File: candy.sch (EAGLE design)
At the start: 4 parts

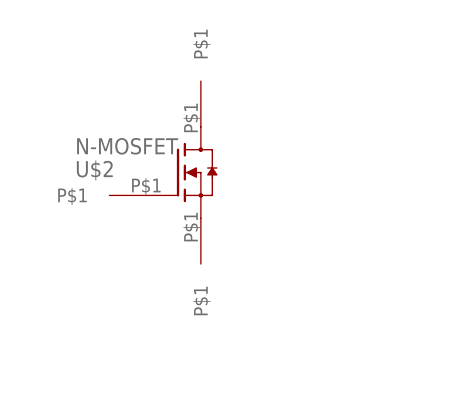
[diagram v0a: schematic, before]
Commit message: has candy, too big pads
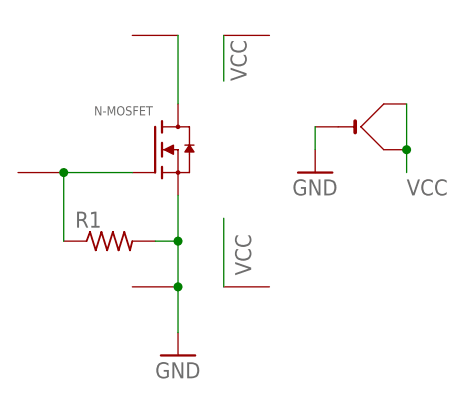
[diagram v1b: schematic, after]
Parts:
- added R1: (no value), adafruit:R-US_R1206
- added U$5, U$6: SMDPAD, TinyTony_ShenzenReady:SMDPAD
- added U$7: (no value), TinyTony_ShenzenReady:CR2032
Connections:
- removed net N$2: U$2.S, U$3.P$1
- new net GND: R1.2, U$2.S, U$3.P$1, U$7.-
- new net VCC: U$5.P$1, U$6.P$1, U$7.+, U$7.+1
- net N$1: now also R1.1
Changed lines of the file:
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@@
 <?xml version="1.0" encoding="utf-8"?>
 <!DOCTYPE eagle SYSTEM "eagle.dtd">
-<eagle version="8.7.0">
+<eagle version="8.6.0">
 <drawing>
 <settings>
@@
 <part name="U$3" library="TinyTony_ShenzenReady" deviceset="SMDPAD" device=""/>
 <part name="U$4" library="TinyTony_ShenzenReady" deviceset="SMDPAD" device=""/>
+<part name="R1" library="adafruit" library_urn="urn:adsk.eagle:library:420" deviceset="R-US_" device="R1206"/>
+<part name="U$5" library="TinyTony_ShenzenReady" deviceset="SMDPAD" device=""/>
+<part name="U$6" library="TinyTony_ShenzenReady" deviceset="SMDPAD" device=""/>
+<part name="U$7" library="TinyTony_ShenzenReady" deviceset="CR2032" device=""/>
+<part name="GND1" library="TinyTony_ShenzenReady" deviceset="GND" device=""/>
+<part name="GND2" library="TinyTony_ShenzenReady" deviceset="GND" device=""/>
 </parts>
 <sheets>
@@
 </plain>
 <instances>
-<instance part="U$1" gate="G$1" x="73.66" y="55.88" rot="R180"/>
-<instance part="U$2" gate="G$1" x="76.2" y="58.42"/>
-<instance part="U$3" gate="G$1" x="78.74" y="53.34" rot="R270"/>
-<instance part="U$4" gate="G$1" x="78.74" y="63.5" rot="R90"/>
+<instance part="U$1" gate="G$1" x="63.5" y="58.42" rot="R180"/>
+<instance part="U$2" gate="G$1" x="73.66" y="60.96" smashed="yes">
+<attribute name="VALUE" x="73.406" y="64.77" size="1.016" layer="96" rot="MR0"/>
+</instance>
+<instance part="U$3" gate="G$1" x="76.2" y="45.72" smashed="yes" rot="R180"/>
+<instance part="U$4" gate="G$1" x="76.2" y="73.66" smashed="yes" rot="R180"/>
+<instance part="R1" gate="G$1" x="68.58" y="50.8"/>
+<instance part="U$5" gate="G$1" x="81.28" y="73.66" smashed="yes"/>
+<instance part="U$6" gate="G$1" x="81.28" y="45.72" smashed="yes"/>
+<instance part="U$7" gate="G$1" x="96.52" y="63.5" smashed="yes">
+<attribute name="VALUE" x="95.25" y="58.42" size="1.778" layer="96"/>
+</instance>
+<instance part="GND1" gate="1" x="91.44" y="58.42"/>
+<instance part="GND2" gate="1" x="76.2" y="38.1"/>
 </instances>
 <busses>
@@
 <pinref part="U$2" gate="G$1" pin="G"/>
 <pinref part="U$1" gate="G$1" pin="P$1"/>
-</segment>
-</net>
-<net name="N$2" class="0">
+<wire x1="63.5" y1="58.42" x2="71.12" y2="58.42" width="0.1524" layer="91"/>
+<pinref part="R1" gate="G$1" pin="1"/>
+<wire x1="63.5" y1="50.8" x2="63.5" y2="58.42" width="0.1524" layer="91"/>
+<junction x="63.5" y="58.42"/>
+</segment>
+</net>
+<net name="N$3" class="0">
+<segment>
+<pinref part="U$2" gate="G$1" pin="D"/>
+<pinref part="U$4" gate="G$1" pin="P$1"/>
+<wire x1="76.2" y1="73.66" x2="76.2" y2="66.04" width="0.1524" layer="91"/>
+</segment>
+</net>
+<net name="GND" class="0">
+<segment>
+<pinref part="U$7" gate="G$1" pin="-"/>
+<pinref part="GND1" gate="1" pin="GND"/>
+<wire x1="91.44" y1="60.96" x2="91.44" y2="63.5" width="0.1524" layer="91"/>
+</segment>
 <segment>
 <pinref part="U$2" gate="G$1" pin="S"/>
 <pinref part="U$3" gate="G$1" pin="P$1"/>
-</segment>
-</net>
-<net name="N$3" class="0">
-<segment>
-<pinref part="U$2" gate="G$1" pin="D"/>
-<pinref part="U$4" gate="G$1" pin="P$1"/>
+<pinref part="R1" gate="G$1" pin="2"/>
+<wire x1="76.2" y1="50.8" x2="76.2" y2="55.88" width="0.1524" layer="91"/>
+<wire x1="76.2" y1="50.8" x2="73.66" y2="50.8" width="0.1524" layer="91"/>
+<junction x="76.2" y="50.8"/>
+<wire x1="76.2" y1="45.72" x2="76.2" y2="50.8" width="0.1524" layer="91"/>
+<pinref part="GND2" gate="1" pin="GND"/>
+<wire x1="76.2" y1="45.72" x2="76.2" y2="40.64" width="0.1524" layer="91"/>
+<junction x="76.2" y="45.72"/>
+</segment>
+</net>
+<net name="VCC" class="0">
+<segment>
+<label x="101.6" y="55.88" size="1.778" layer="95"/>
+<pinref part="U$7" gate="G$1" pin="+1"/>
+<wire x1="101.6" y1="60.96" x2="101.6" y2="58.42" width="0.1524" layer="91"/>
+<pinref part="U$7" gate="G$1" pin="+"/>
+<wire x1="101.6" y1="66.04" x2="101.6" y2="60.96" width="0.1524" layer="91"/>
+<junction x="101.6" y="60.96"/>
+</segment>
+<segment>
+<pinref part="U$5" gate="G$1" pin="P$1"/>
+<wire x1="81.28" y1="73.66" x2="81.28" y2="68.58" width="0.1524" layer="91"/>
+<label x="82.042" y="73.152" size="1.778" layer="95" rot="R270"/>
+</segment>
+<segment>
+<pinref part="U$6" gate="G$1" pin="P$1"/>
+<wire x1="81.28" y1="45.72" x2="81.28" y2="53.34" width="0.1524" layer="91"/>
+<label x="82.55" y="51.562" size="1.778" layer="95" rot="R270"/>
 </segment>
 </net>
@@
 </drawing>
 <compatibility>
+<note version="8.2" severity="warning">
+Since Version 8.2, EAGLE supports online libraries. The ids
+of those online libraries will not be understood (or retained)
+with this version.
+</note>
 <note version="8.3" severity="warning">
 Since Version 8.3, EAGLE supports URNs for individual library

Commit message: sch
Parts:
- U$2: value N-MOSFET -> N-MOSFETREGULAR; device TinyTony_ShenzenReady:N-MOSFET -> TinyTony_ShenzenReady:N-MOSFETREGULAR
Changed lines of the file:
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@@
 <parts>
 <part name="U$1" library="TinyTony_ShenzenReady" deviceset="SMDPAD" device=""/>
-<part name="U$2" library="TinyTony_ShenzenReady" deviceset="N-MOSFET" device=""/>
+<part name="U$2" library="TinyTony_ShenzenReady" deviceset="N-MOSFET" device="REGULAR" value="N-MOSFETREGULAR"/>
 <part name="U$3" library="TinyTony_ShenzenReady" deviceset="SMDPAD" device=""/>
 <part name="U$4" library="TinyTony_ShenzenReady" deviceset="SMDPAD" device=""/>

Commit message: with ugly polygons on layout
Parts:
- U$7: device TinyTony_ShenzenReady:CR2032 -> TinyTony_ShenzenReady:CR2032LINX
- renumbered U$6 to VCC
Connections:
- net VCC: no longer U$7.+1
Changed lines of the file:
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@@
 <?xml version="1.0" encoding="utf-8"?>
 <!DOCTYPE eagle SYSTEM "eagle.dtd">
-<eagle version="8.6.0">
+<eagle version="8.7.0">
 <drawing>
 <settings>
@@
 <grid distance="0.1" unitdist="inch" unit="inch" style="lines" multiple="1" display="no" altdistance="0.01" altunitdist="inch" altunit="inch"/>
 <layers>
-<layer number="1" name="Top" color="4" fill="1" visible="no" active="no"/>
-<layer number="16" name="Bottom" color="1" fill="1" visible="no" active="no"/>
-<layer number="17" name="Pads" color="2" fill="1" visible="no" active="no"/>
-<layer number="18" name="Vias" color="2" fill="1" visible="no" active="no"/>
-<layer number="19" name="Unrouted" color="6" fill="1" visible="no" active="no"/>
-<layer number="20" name="Dimension" color="15" fill="1" visible="no" active="no"/>
-<layer number="21" name="tPlace" color="7" fill="1" visible="no" active="no"/>
-<layer number="22" name="bPlace" color="7" fill="1" visible="no" active="no"/>
-<layer number="23" name="tOrigins" color="15" fill="1" visible="no" active="no"/>
-<layer number="24" name="bOrigins" color="15" fill="1" visible="no" active="no"/>
-<layer number="25" name="tNames" color="7" fill="1" visible="no" active="no"/>
-<layer number="26" name="bNames" color="7" fill="1" visible="no" active="no"/>
-<layer number="27" name="tValues" color="7" fill="1" visible="no" active="no"/>
-<layer number="28" name="bValues" color="7" fill="1" visible="no" active="no"/>
+<layer number="1" name="Top" color="4" fill="1" visible="yes" active="no"/>
+<layer number="16" name="Bottom" color="1" fill="1" visible="yes" active="no"/>
+<layer number="17" name="Pads" color="2" fill="1" visible="yes" active="no"/>
+<layer number="18" name="Vias" color="2" fill="1" visible="yes" active="no"/>
+<layer number="19" name="Unrouted" color="6" fill="1" visible="yes" active="no"/>
+<layer number="20" name="Dimension" color="24" fill="1" visible="yes" active="no"/>
+<layer number="21" name="tPlace" color="7" fill="1" visible="yes" active="no"/>
+<layer number="22" name="bPlace" color="7" fill="1" visible="yes" active="no"/>
+<layer number="23" name="tOrigins" color="15" fill="1" visible="yes" active="no"/>
+<layer number="24" name="bOrigins" color="15" fill="1" visible="yes" active="no"/>
+<layer number="25" name="tNames" color="7" fill="1" visible="yes" active="no"/>
+<layer number="26" name="bNames" color="7" fill="1" visible="yes" active="no"/>
+<layer number="27" name="tValues" color="7" fill="1" visible="yes" active="no"/>
+<layer number="28" name="bValues" color="7" fill="1" visible="yes" active="no"/>
 <layer number="29" name="tStop" color="7" fill="3" visible="no" active="no"/>
 <layer number="30" name="bStop" color="7" fill="6" visible="no" active="no"/>
@@
 <layer number="35" name="tGlue" color="7" fill="4" visible="no" active="no"/>
 <layer number="36" name="bGlue" color="7" fill="5" visible="no" active="no"/>
-<layer number="37" name="tTest" color="7" fill="1" visible="no" active="no"/>
-<layer number="38" name="bTest" color="7" fill="1" visible="no" active="no"/>
+<layer number="37" name="tTest" color="7" fill="1" visible="yes" active="no"/>
+<layer number="38" name="bTest" color="7" fill="1" visible="yes" active="no"/>
 <layer number="39" name="tKeepout" color="4" fill="11" visible="no" active="no"/>
 <layer number="40" name="bKeepout" color="1" fill="11" visible="no" active="no"/>
@@
 <layer number="44" name="Drills" color="7" fill="1" visible="no" active="no"/>
 <layer number="45" name="Holes" color="7" fill="1" visible="no" active="no"/>
-<layer number="46" name="Milling" color="3" fill="1" visible="no" active="no"/>
-<layer number="47" name="Measures" color="7" fill="1" visible="no" active="no"/>
-<layer number="48" name="Document" color="7" fill="1" visible="no" active="no"/>
-<layer number="49" name="Reference" color="7" fill="1" visible="no" active="no"/>
-<layer number="50" name="dxf" color="7" fill="1" visible="no" active="no"/>
-<layer number="51" name="tDocu" color="7" fill="1" visible="no" active="no"/>
-<layer number="52" name="bDocu" color="7" fill="1" visible="no" active="no"/>
-<layer number="53" name="tGND_GNDA" color="7" fill="1" visible="no" active="no"/>
-<layer number="54" name="bGND_GNDA" color="7" fill="1" visible="no" active="no"/>
-<layer number="56" name="wert" color="7" fill="1" visible="no" active="no"/>
-<layer number="57" name="tCAD" color="7" fill="1" visible="no" active="no"/>
-<layer number="59" name="tCarbon" color="7" fill="1" visible="no" active="no"/>
-<layer number="60" name="bCarbon" color="7" fill="1" visible="no" active="no"/>
+<layer number="46" name="Milling" color="3" fill="1" visible="yes" active="no"/>
+<layer number="47" name="Measures" color="7" fill="1" visible="yes" active="no"/>
+<layer number="48" name="Document" color="7" fill="1" visible="yes" active="no"/>
+<layer number="49" name="Reference" color="7" fill="1" visible="yes" active="no"/>
+<layer number="50" name="dxf" color="7" fill="1" visible="yes" active="no"/>
+<layer number="51" name="tDocu" color="7" fill="1" visible="yes" active="no"/>
+<layer number="52" name="bDocu" color="7" fill="1" visible="yes" active="no"/>
+<layer number="53" name="tGND_GNDA" color="7" fill="1" visible="yes" active="no"/>
+<layer number="54" name="bGND_GNDA" color="7" fill="1" visible="yes" active="no"/>
+<layer number="56" name="wert" color="7" fill="1" visible="yes" active="no"/>
+<layer number="57" name="tCAD" color="7" fill="1" visible="yes" active="no"/>
+<layer number="59" name="tCarbon" color="7" fill="1" visible="yes" active="no"/>
+<layer number="60" name="bCarbon" color="7" fill="1" visible="yes" active="no"/>
 <layer number="88" name="SimResults" color="9" fill="1" visible="yes" active="yes"/>
 <layer number="89" name="SimProbes" color="9" fill="1" visible="yes" active="yes"/>
@@
 <part name="R1" library="adafruit" library_urn="urn:adsk.eagle:library:420" deviceset="R-US_" device="R1206"/>
 <part name="U$5" library="TinyTony_ShenzenReady" deviceset="SMDPAD" device=""/>
-<part name="U$6" library="TinyTony_ShenzenReady" deviceset="SMDPAD" device=""/>
-<part name="U$7" library="TinyTony_ShenzenReady" deviceset="CR2032" device=""/>
+<part name="VCC" library="TinyTony_ShenzenReady" deviceset="SMDPAD" device=""/>
+<part name="U$7" library="TinyTony_ShenzenReady" library_urn="urn:adsk.eagle:library:2159173" deviceset="CR2032" device="LINX" package3d_urn="urn:adsk.eagle:package:2160680/2"/>
 <part name="GND1" library="TinyTony_ShenzenReady" deviceset="GND" device=""/>
 <part name="GND2" library="TinyTony_ShenzenReady" deviceset="GND" device=""/>
@@
 <instance part="R1" gate="G$1" x="68.58" y="50.8"/>
 <instance part="U$5" gate="G$1" x="81.28" y="73.66" smashed="yes"/>
-<instance part="U$6" gate="G$1" x="81.28" y="45.72" smashed="yes"/>
+<instance part="VCC" gate="G$1" x="81.28" y="45.72" smashed="yes"/>
 <instance part="U$7" gate="G$1" x="96.52" y="63.5" smashed="yes">
 <attribute name="VALUE" x="95.25" y="58.42" size="1.778" layer="96"/>
@@
 <net name="VCC" class="0">
 <segment>
-<label x="101.6" y="55.88" size="1.778" layer="95"/>
-<pinref part="U$7" gate="G$1" pin="+1"/>
-<wire x1="101.6" y1="60.96" x2="101.6" y2="58.42" width="0.1524" layer="91"/>
-<pinref part="U$7" gate="G$1" pin="+"/>
-<wire x1="101.6" y1="66.04" x2="101.6" y2="60.96" width="0.1524" layer="91"/>
-<junction x="101.6" y="60.96"/>
-</segment>
-<segment>
 <pinref part="U$5" gate="G$1" pin="P$1"/>
 <wire x1="81.28" y1="73.66" x2="81.28" y2="68.58" width="0.1524" layer="91"/>
@@
 </segment>
 <segment>
-<pinref part="U$6" gate="G$1" pin="P$1"/>
+<pinref part="VCC" gate="G$1" pin="P$1"/>
 <wire x1="81.28" y1="45.72" x2="81.28" y2="53.34" width="0.1524" layer="91"/>
 <label x="82.55" y="51.562" size="1.778" layer="95" rot="R270"/>
+</segment>
+<segment>
+<pinref part="U$7" gate="G$1" pin="+"/>
+<wire x1="101.6" y1="63.5" x2="106.68" y2="63.5" width="0.1524" layer="91"/>
+<wire x1="106.68" y1="63.5" x2="106.68" y2="58.42" width="0.1524" layer="91"/>
+<label x="106.68" y="55.88" size="1.778" layer="95"/>
 </segment>
 </net>
@@
 will not be understood (or retained) with this version.
 </note>
+<note version="8.3" severity="warning">
+Since Version 8.3, EAGLE supports the association of 3D packages
+with devices in libraries, schematics, and board files. Those 3D
+packages will not be understood (or retained) with this version.
+</note>
 </compatibility>

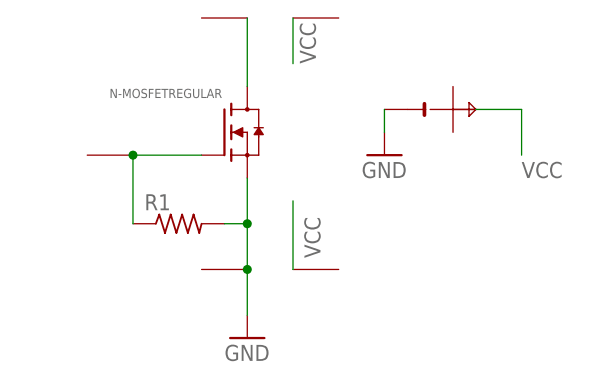
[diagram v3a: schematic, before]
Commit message: fixed schema and added 2n222
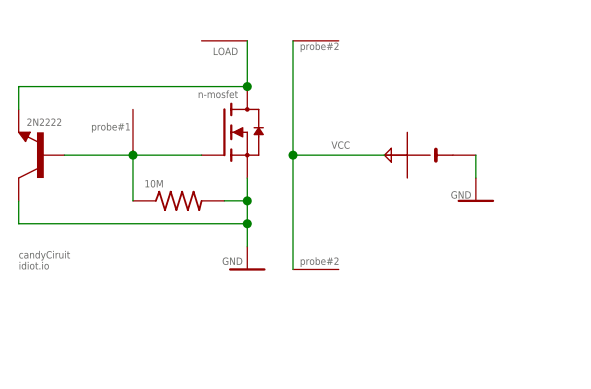
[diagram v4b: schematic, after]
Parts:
- removed R1: (no value), adafruit:R-US_R1206
- removed U$3: SMDPAD, TinyTony_ShenzenReady:SMDPAD
- added 10M: (no value), adafruit:R-US_R1206
- added 2N2222: (no value), transistor-neu-to92:2N2222-NPN-TO92-EBC
- N-MOSFET: value N-MOSFETREGULAR -> n-mosfet
- renumbered U$2 to N-MOSFET
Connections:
- removed net N$3: N-MOSFET.D, U$4.P$1
- new net LOAD: 2N2222.E, N-MOSFET.D, U$4.P$1
- net GND: now also 10M.2, 2N2222.C; no longer R1.2, U$3.P$1
- net N$1: now also 10M.1, 2N2222.B; no longer R1.1
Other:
- note added: "candyCiruit idiot.io"
- note added: "probe#1"
- note added: "probe#2"

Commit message: board ready for silk
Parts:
- 2N2222: device transistor-neu-to92:2N2222-NPN-TO92-EBC -> TinyTony_ShenzenReady:2N2222-NPN-TO92-EBC
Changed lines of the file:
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@@
 <grid distance="0.1" unitdist="inch" unit="inch" style="lines" multiple="1" display="no" altdistance="0.01" altunitdist="inch" altunit="inch"/>
 <layers>
-<layer number="1" name="Top" color="4" fill="1" visible="no" active="no"/>
-<layer number="16" name="Bottom" color="1" fill="1" visible="no" active="no"/>
-<layer number="17" name="Pads" color="2" fill="1" visible="no" active="no"/>
-<layer number="18" name="Vias" color="2" fill="1" visible="no" active="no"/>
-<layer number="19" name="Unrouted" color="6" fill="1" visible="no" active="no"/>
-<layer number="20" name="Dimension" color="24" fill="1" visible="no" active="no"/>
-<layer number="21" name="tPlace" color="7" fill="1" visible="no" active="no"/>
-<layer number="22" name="bPlace" color="7" fill="1" visible="no" active="no"/>
-<layer number="23" name="tOrigins" color="15" fill="1" visible="no" active="no"/>
-<layer number="24" name="bOrigins" color="15" fill="1" visible="no" active="no"/>
-<layer number="25" name="tNames" color="7" fill="1" visible="no" active="no"/>
-<layer number="26" name="bNames" color="7" fill="1" visible="no" active="no"/>
-<layer number="27" name="tValues" color="7" fill="1" visible="no" active="no"/>
-<layer number="28" name="bValues" color="7" fill="1" visible="no" active="no"/>
+<layer number="1" name="Top" color="4" fill="1" visible="yes" active="no"/>
+<layer number="16" name="Bottom" color="1" fill="1" visible="yes" active="no"/>
+<layer number="17" name="Pads" color="2" fill="1" visible="yes" active="no"/>
+<layer number="18" name="Vias" color="2" fill="1" visible="yes" active="no"/>
+<layer number="19" name="Unrouted" color="6" fill="1" visible="yes" active="no"/>
+<layer number="20" name="Dimension" color="24" fill="1" visible="yes" active="no"/>
+<layer number="21" name="tPlace" color="7" fill="1" visible="yes" active="no"/>
+<layer number="22" name="bPlace" color="7" fill="1" visible="yes" active="no"/>
+<layer number="23" name="tOrigins" color="15" fill="1" visible="yes" active="no"/>
+<layer number="24" name="bOrigins" color="15" fill="1" visible="yes" active="no"/>
+<layer number="25" name="tNames" color="7" fill="1" visible="yes" active="no"/>
+<layer number="26" name="bNames" color="7" fill="1" visible="yes" active="no"/>
+<layer number="27" name="tValues" color="7" fill="1" visible="yes" active="no"/>
+<layer number="28" name="bValues" color="7" fill="1" visible="yes" active="no"/>
 <layer number="29" name="tStop" color="7" fill="3" visible="no" active="no"/>
 <layer number="30" name="bStop" color="7" fill="6" visible="no" active="no"/>
@@
 <layer number="35" name="tGlue" color="7" fill="4" visible="no" active="no"/>
 <layer number="36" name="bGlue" color="7" fill="5" visible="no" active="no"/>
-<layer number="37" name="tTest" color="7" fill="1" visible="no" active="no"/>
-<layer number="38" name="bTest" color="7" fill="1" visible="no" active="no"/>
+<layer number="37" name="tTest" color="7" fill="1" visible="yes" active="no"/>
+<layer number="38" name="bTest" color="7" fill="1" visible="yes" active="no"/>
 <layer number="39" name="tKeepout" color="4" fill="11" visible="no" active="no"/>
 <layer number="40" name="bKeepout" color="1" fill="11" visible="no" active="no"/>
@@
 <layer number="44" name="Drills" color="7" fill="1" visible="no" active="no"/>
 <layer number="45" name="Holes" color="7" fill="1" visible="no" active="no"/>
-<layer number="46" name="Milling" color="3" fill="1" visible="no" active="no"/>
-<layer number="47" name="Measures" color="7" fill="1" visible="no" active="no"/>
-<layer number="48" name="Document" color="7" fill="1" visible="no" active="no"/>
-<layer number="49" name="Reference" color="7" fill="1" visible="no" active="no"/>
-<layer number="50" name="dxf" color="7" fill="1" visible="no" active="no"/>
-<layer number="51" name="tDocu" color="7" fill="1" visible="no" active="no"/>
-<layer number="52" name="bDocu" color="7" fill="1" visible="no" active="no"/>
-<layer number="53" name="tGND_GNDA" color="7" fill="1" visible="no" active="no"/>
-<layer number="54" name="bGND_GNDA" color="7" fill="1" visible="no" active="no"/>
-<layer number="56" name="wert" color="7" fill="1" visible="no" active="no"/>
-<layer number="57" name="tCAD" color="7" fill="1" visible="no" active="no"/>
-<layer number="59" name="tCarbon" color="7" fill="1" visible="no" active="no"/>
-<layer number="60" name="bCarbon" color="7" fill="1" visible="no" active="no"/>
+<layer number="46" name="Milling" color="3" fill="1" visible="yes" active="no"/>
+<layer number="47" name="Measures" color="7" fill="1" visible="yes" active="no"/>
+<layer number="48" name="Document" color="7" fill="1" visible="yes" active="no"/>
+<layer number="49" name="Reference" color="7" fill="1" visible="yes" active="no"/>
+<layer number="50" name="dxf" color="7" fill="1" visible="yes" active="no"/>
+<layer number="51" name="tDocu" color="7" fill="1" visible="yes" active="no"/>
+<layer number="52" name="bDocu" color="7" fill="1" visible="yes" active="no"/>
+<layer number="53" name="tGND_GNDA" color="7" fill="1" visible="yes" active="no"/>
+<layer number="54" name="bGND_GNDA" color="7" fill="1" visible="yes" active="no"/>
+<layer number="56" name="wert" color="7" fill="1" visible="yes" active="no"/>
+<layer number="57" name="tCAD" color="7" fill="1" visible="yes" active="no"/>
+<layer number="59" name="tCarbon" color="7" fill="1" visible="yes" active="no"/>
+<layer number="60" name="bCarbon" color="7" fill="1" visible="yes" active="no"/>
 <layer number="88" name="SimResults" color="9" fill="1" visible="yes" active="yes"/>
 <layer number="89" name="SimProbes" color="9" fill="1" visible="yes" active="yes"/>
@@
 <part name="GND1" library="TinyTony_ShenzenReady" deviceset="GND" device=""/>
 <part name="GND2" library="TinyTony_ShenzenReady" deviceset="GND" device=""/>
-<part name="2N2222" library="transistor-neu-to92" library_urn="urn:adsk.eagle:library:397" deviceset="*-NPN-" device="TO92-EBC" package3d_urn="urn:adsk.eagle:package:28763/2" technology="2N2222"/>
+<part name="2N2222" library="TinyTony_ShenzenReady" library_urn="urn:adsk.eagle:library:2159173" deviceset="*-NPN-" device="TO92-EBC" package3d_urn="urn:adsk.eagle:package:28763/2" technology="2N2222"/>
 <part name="FRAME1" library="TinyTony_ShenzenReady" library_urn="urn:adsk.eagle:library:2159173" deviceset="A4L-LOC" device=""/>
 </parts>
